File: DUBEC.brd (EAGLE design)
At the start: 39 x 21.4 mm, 53 parts

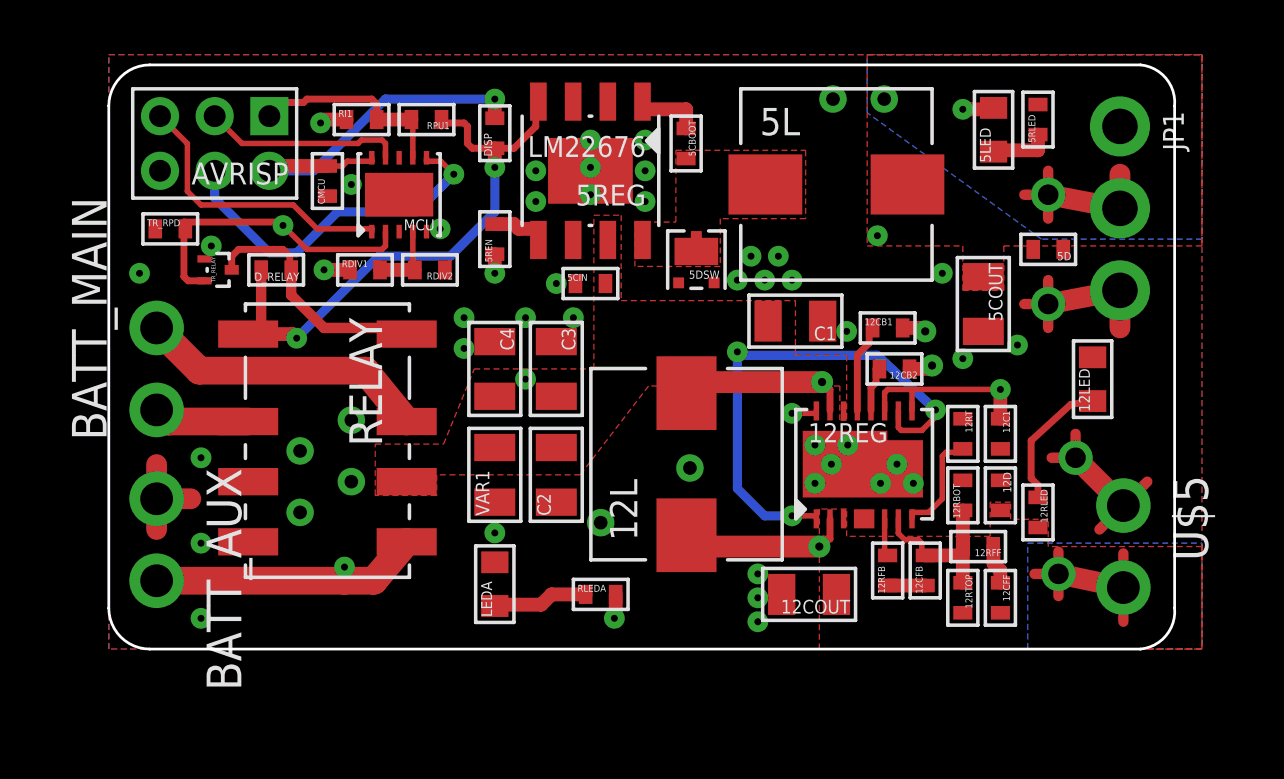
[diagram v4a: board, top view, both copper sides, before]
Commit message: Second 12V ceramic cap
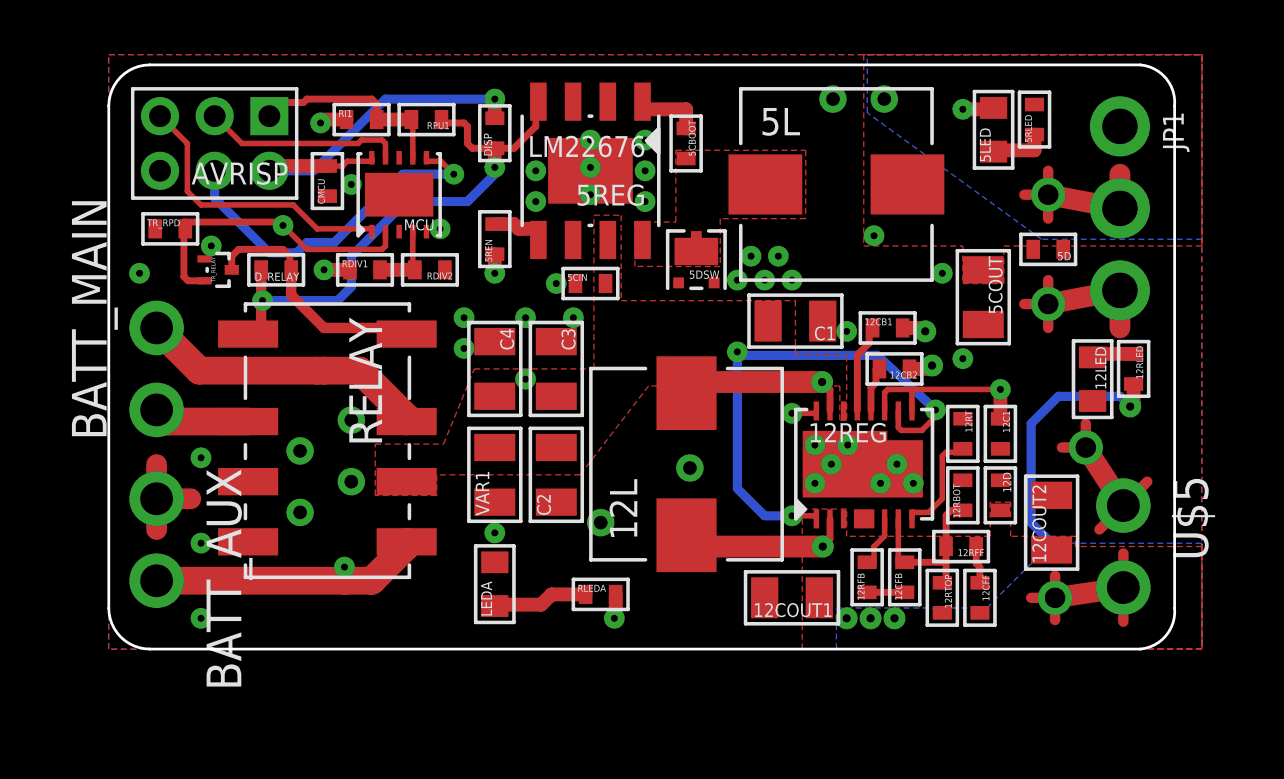
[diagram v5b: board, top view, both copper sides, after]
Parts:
- removed 12COUT: 22uF, dubec:0805
- added 12COUT1, 12COUT2: 22uF, dubec:0805
- moved 12RLED 6.31 mm to (37.5, 10.2)
- moved U$3 0.88 mm to (34.6, 1.88)
- moved 12CFB 0.79 mm to (29.1, 2.62)
- moved 12RFB 0.79 mm to (27.8, 2.62)
- moved 12CFF 0.75 mm to (31.9, 1.88)
- moved 12RTOP 0.75 mm to (30.5, 1.88)
- moved 12RFF 0.62 mm to (31.2, 3.75)
- moved U$4 0.53 mm to (35.8, 7.38)
- moved 5COUT 0.25 mm to (32.0, 12.9)
- moved 5RLED 0.12 mm to (33.9, 19.4)
- turned 12LED to 270 degrees
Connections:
- net 12V: now also 12COUT1.1, 12COUT2.1; no longer 12COUT.1
- net GND: now also 12COUT1.2, 12COUT2.2; no longer 12COUT.2
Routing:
- net 12V: track 7.43 -> 17.3 mm, vias 0 -> 4
- net N$7: track 4.95 -> 1.55 mm
- net 5V: track 42.5 -> 41.7 mm
- net 12V_COMP: track 1.47 -> 2.00 mm
- net GND: vias 48 -> 44
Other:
- board text added: "3..8S"
- board text added: "Input: 3..8 cell LiPo Output: 5V/3A + 12V/1.4A By TURBOFUNCTION.com/fpv"
- board text removed: "3-8S"
- board text removed: "Input: 3..8S Output: 5V/3A + 12V/1.4A By TURBOFUNCTION.com/fpv"

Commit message: Tidying
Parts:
- moved DISP 1.50 mm to (14.1, 17.4), turned to 270 degrees
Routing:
- net 12VCC: track 20.5 -> 13.7 mm
- net 12V: track 17.3 -> 19.0 mm
- net 5V_ISP: track 14.1 -> 12.9 mm
- net 5V: track 41.7 -> 40.6 mm
- net N$3: track 9.75 -> 10.3 mm
- net GND: vias 44 -> 48

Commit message: Routing
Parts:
- moved 12RLED 4.75 mm to (32.8, 10.2)
- moved 12C1 3.41 mm to (31.2, 11.0), turned to 90 degrees
- moved 5RLED 2.75 mm to (31.1, 19.5), turned to 270 degrees
- moved 12D 2.25 mm to (32.8, 7.88)
- moved 5LED 2.13 mm to (34.5, 19.1), turned to 270 degrees
- moved 5COUT 1.75 mm to (32.0, 14.6)
- moved 12LED 1.12 mm to (37.1, 9.88)
- moved 12COUT2 0.76 mm to (33.8, 4.75)
- moved 12CFB 0.38 mm to (29.1, 3.00)
- moved 12RFB 0.38 mm to (27.8, 3.00)
- moved U$1 0.28 mm to (34.2, 16.4)
- moved U$3 0.28 mm to (34.4, 1.75)
- moved U$4 0.28 mm to (35.6, 7.12)
- moved U$2 0.18 mm to (34.2, 12.8)
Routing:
- net 12V: track 19.0 -> 15.1 mm, vias 4 -> 2
- net N$7: track 1.55 -> 4.43 mm
- net 5V_ISP: track 12.9 -> 15.0 mm
- net 5V_PG: track 1.93 -> 3.43 mm
- net 12VCC: track 13.7 -> 12.5 mm
- net 35V: track 23.9 -> 25.0 mm
- net GND: track 17.2 -> 18.3 mm, vias 48 -> 47
- net 12V_FB: track 6.79 -> 6.16 mm
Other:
- board text added: "Input: 3..8 LiPo cells Output: 5V/3A + 12V/1.4A By TURBOFUNCTION.com/fpv"
- board text removed: "Input: 3..8 cell LiPo Output: 5V/3A + 12V/1.4A By TURBOFUNCTION.com/fpv"

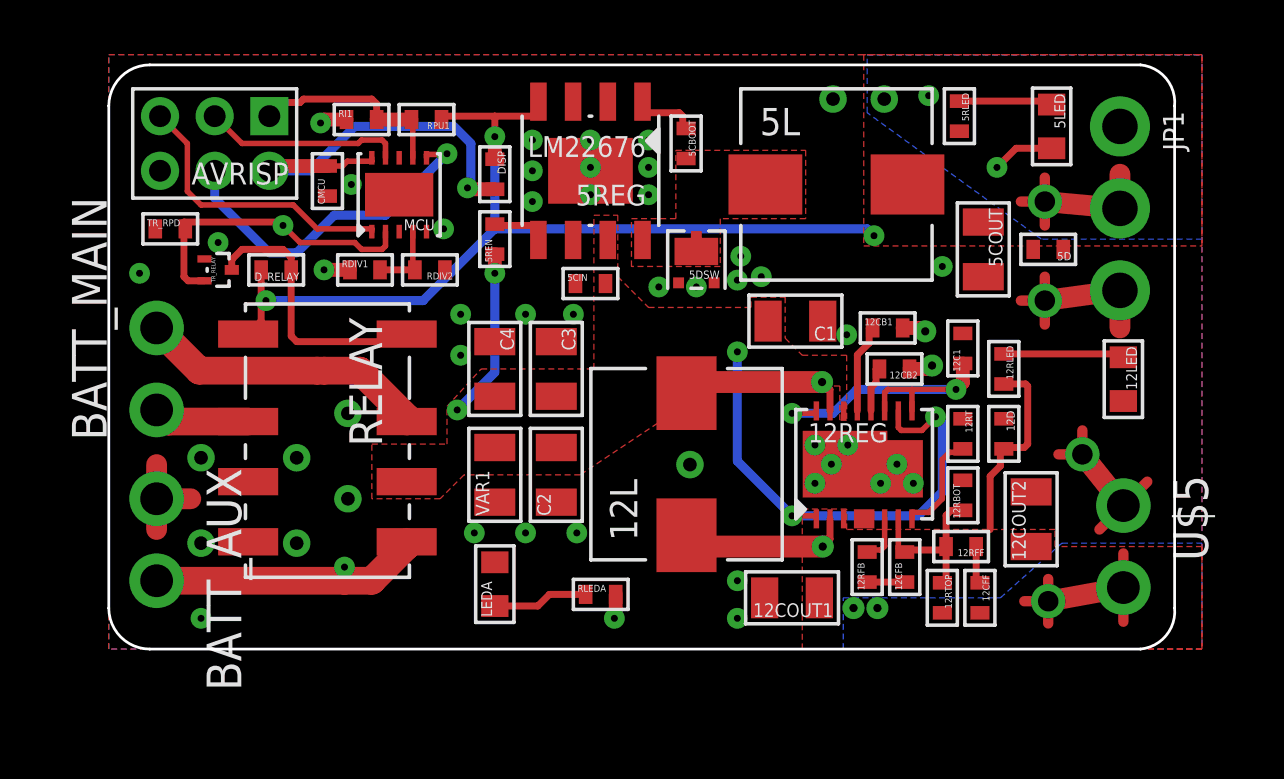
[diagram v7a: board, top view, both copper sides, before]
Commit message: Layout tweaks
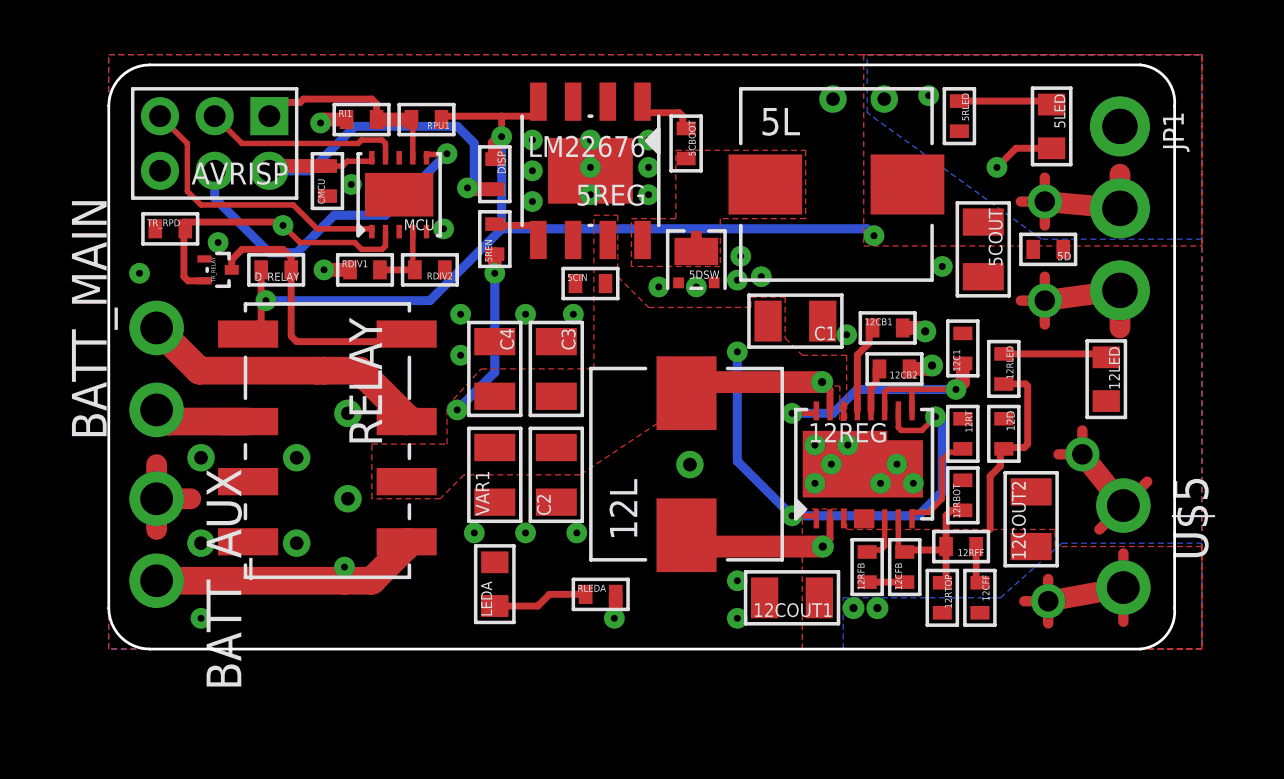
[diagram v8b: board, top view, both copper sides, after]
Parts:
- moved 12LED 0.62 mm to (36.5, 9.88)
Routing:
- net N$7: track 4.43 -> 3.80 mm
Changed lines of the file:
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@@
 <wire x1="0" y1="19.875" x2="0" y2="1.5" width="0.1" layer="20"/>
 <text x="8.125" y="2" size="1.27" layer="107" font="vector" ratio="20" rot="SR0" align="top-center">3..8S</text>
-<text x="36" y="9.875" size="1.27" layer="107" font="vector" ratio="20" rot="SR90" align="bottom-center">12V</text>
+<text x="35.375" y="9.875" size="1.27" layer="107" font="vector" ratio="20" rot="SR90" align="bottom-center">12V</text>
 <text x="33.375" y="19.125" size="1.25" layer="107" font="vector" ratio="20" rot="R90" align="bottom-center">5V</text>
 <text x="15.25" y="2.375" size="1.27" layer="107" font="vector" ratio="20" rot="SR270" align="bottom-center">AUX</text>
@@
 <attribute name="USD" value="0.44" x="34.5" y="19.125" size="1.778" layer="27" rot="R270" display="off"/>
 </element>
-<element name="12LED" library="dubec" package="D0603" value="LEDGREEN_2.8V_5MA" x="37.125" y="9.875" rot="R270">
-<attribute name="DIGIKEY_PART_#" value="160-1832-1-ND" x="37.125" y="9.875" size="1.778" layer="27" rot="R270" display="off"/>
-<attribute name="MANUFACTURER" value="Lite-On Inc" x="37.125" y="9.875" size="1.778" layer="27" rot="R270" display="off"/>
-<attribute name="TYPE" value="smt" x="37.125" y="9.875" size="1.778" layer="27" rot="R270" display="off"/>
-<attribute name="MFG_PART_#" value="LTST-C193TGKT-5A" x="37.125" y="9.875" size="1.778" layer="27" rot="R270" display="off"/>
-<attribute name="USD" value="0.44" x="37.125" y="9.875" size="1.778" layer="27" rot="R270" display="off"/>
+<element name="12LED" library="dubec" package="D0603" value="LEDGREEN_2.8V_5MA" x="36.5" y="9.875" rot="R270">
+<attribute name="DIGIKEY_PART_#" value="160-1832-1-ND" x="36.5" y="9.875" size="1.778" layer="27" rot="R270" display="off"/>
+<attribute name="MANUFACTURER" value="Lite-On Inc" x="36.5" y="9.875" size="1.778" layer="27" rot="R270" display="off"/>
+<attribute name="TYPE" value="smt" x="36.5" y="9.875" size="1.778" layer="27" rot="R270" display="off"/>
+<attribute name="MFG_PART_#" value="LTST-C193TGKT-5A" x="36.5" y="9.875" size="1.778" layer="27" rot="R270" display="off"/>
+<attribute name="USD" value="0.44" x="36.5" y="9.875" size="1.778" layer="27" rot="R270" display="off"/>
 </element>
 <element name="LEDA" library="dubec" package="D0603" value="LEDGREEN_2.8V_5MA" x="14.125" y="2.375" rot="R90">
@@
 <vertex x="27.625" y="21.75"/>
 </polygon>
-<via x="14.125" y="18.75" extent="1-16" drill="0.254"/>
+<via x="14.375" y="18.75" extent="1-16" drill="0.254"/>
 <via x="5.75" y="12.75" extent="1-16" drill="0.254"/>
 <contactref element="5D" pad="C"/>
@@
 <wire x1="37" y1="17.375" x2="37" y2="17.125" width="0.762" layer="1"/>
 <wire x1="34.25" y1="16.375" x2="33.375" y2="16.375" width="0.381" layer="1"/>
-<wire x1="14.125" y1="17.925" x2="14.125" y2="18.75" width="0.508" layer="1"/>
+<wire x1="14.125" y1="17.925" x2="14.125" y2="18.5" width="0.508" layer="1"/>
+<wire x1="14.125" y1="18.5" x2="14.375" y2="18.75" width="0.508" layer="1"/>
 <wire x1="34.25" y1="17.25" x2="34.25" y2="16.375" width="0.381" layer="1"/>
 <wire x1="34.25" y1="16.375" x2="34.25" y2="15.5" width="0.381" layer="1"/>
@@
 <wire x1="12.175" y1="19.5" x2="12.175" y2="19.375" width="0.254" layer="1"/>
 <wire x1="5.575" y1="12" x2="5.1" y2="11.525" width="0.254" layer="1"/>
-<wire x1="14.125" y1="15.375" x2="27.75" y2="15.375" width="0.3302" layer="16"/>
+<wire x1="14.375" y1="15.375" x2="27.75" y2="15.375" width="0.3302" layer="16"/>
 <wire x1="27.75" y1="15.375" x2="28" y2="15.125" width="0.3302" layer="16"/>
-<wire x1="14.125" y1="18.75" x2="14.125" y2="15.375" width="0.3302" layer="16"/>
-<wire x1="12.175" y1="19.5" x2="14.125" y2="19.5" width="0.254" layer="1"/>
+<wire x1="14.375" y1="18.75" x2="14.375" y2="15.375" width="0.3302" layer="16"/>
+<wire x1="12.175" y1="19.5" x2="14.375" y2="19.5" width="0.254" layer="1"/>
 <wire x1="15.72" y1="20.03" x2="15.72" y2="19.5" width="0.254" layer="1"/>
-<wire x1="15.72" y1="19.5" x2="14.125" y2="19.5" width="0.254" layer="1"/>
-<wire x1="14.125" y1="15.375" x2="11.5" y2="12.75" width="0.3302" layer="16"/>
-<wire x1="11.5" y1="12.75" x2="5.75" y2="12.75" width="0.3302" layer="16"/>
-<wire x1="14.125" y1="18.75" x2="14.125" y2="19.5" width="0.254" layer="1"/>
+<wire x1="15.72" y1="19.5" x2="14.375" y2="19.5" width="0.254" layer="1"/>
+<wire x1="14.375" y1="15.375" x2="11.75" y2="12.75" width="0.3302" layer="16"/>
+<wire x1="11.75" y1="12.75" x2="5.75" y2="12.75" width="0.3302" layer="16"/>
+<wire x1="14.375" y1="18.75" x2="14.375" y2="19.5" width="0.254" layer="1"/>
 <wire x1="5.75" y1="12.75" x2="5.575" y2="12" width="0" layer="19" extent="1-1"/>
 </signal>
@@
 <wire x1="20.125" y1="19.625" x2="8.125" y2="19.625" width="0.3302" layer="15"/>
 <wire x1="8.125" y1="19.625" x2="7.75" y2="19.25" width="0.3302" layer="15"/>
-<wire x1="20.125" y1="19.625" x2="21" y2="18.75" width="0.3302" layer="15"/>
-<wire x1="21" y1="18.75" x2="36.625" y2="18.75" width="0.3302" layer="15"/>
+<wire x1="20.125" y1="19.625" x2="20.875" y2="18.875" width="0.3302" layer="15"/>
+<wire x1="20.875" y1="18.875" x2="36.75" y2="18.875" width="0.3302" layer="15"/>
 <wire x1="8.7" y1="19.375" x2="7.875" y2="19.375" width="0.508" layer="1"/>
 <wire x1="7.875" y1="19.375" x2="7.75" y2="19.25" width="0.508" layer="1"/>
-<wire x1="36.625" y1="18.75" x2="37" y2="19.125" width="0.3302" layer="15"/>
+<wire x1="36.75" y1="18.875" x2="37" y2="19.125" width="0.3302" layer="15"/>
 </signal>
 <signal name="5V_ISP">
@@
 <wire x1="13.125" y1="16.875" x2="13.175" y2="16.825" width="0.508" layer="1"/>
 <wire x1="13.175" y1="16.825" x2="14.125" y2="16.825" width="0.508" layer="1"/>
-<wire x1="13.125" y1="16.875" x2="13.25" y2="17" width="0.3302" layer="16"/>
-<wire x1="13.25" y1="17" x2="13.25" y2="18.5" width="0.3302" layer="16"/>
-<wire x1="13.25" y1="18.5" x2="12.625" y2="19.125" width="0.3302" layer="16"/>
-<wire x1="12.625" y1="19.125" x2="9" y2="19.125" width="0.3302" layer="16"/>
+<wire x1="13.125" y1="16.875" x2="13.375" y2="17.125" width="0.3302" layer="16"/>
+<wire x1="13.375" y1="17.125" x2="13.375" y2="18.5" width="0.3302" layer="16"/>
+<wire x1="13.375" y1="18.5" x2="12.75" y2="19.125" width="0.3302" layer="16"/>
+<wire x1="12.75" y1="19.125" x2="9" y2="19.125" width="0.3302" layer="16"/>
 <wire x1="9" y1="19.125" x2="7.375" y2="17.5" width="0.3302" layer="16"/>
 <wire x1="7.375" y1="17.5" x2="5.875" y2="17.5" width="0.3302" layer="16"/>
@@
 <contactref element="12LED" pad="A"/>
 <contactref element="12RLED" pad="1"/>
-<wire x1="32.75" y1="10.8" x2="37" y2="10.8" width="0.254" layer="1"/>
-<wire x1="37" y1="10.8" x2="37.125" y2="10.675" width="0.254" layer="1"/>
+<wire x1="32.75" y1="10.8" x2="36.375" y2="10.8" width="0.254" layer="1"/>
+<wire x1="36.375" y1="10.8" x2="36.5" y2="10.675" width="0.254" layer="1"/>
 </signal>
 <signal name="SCK">
